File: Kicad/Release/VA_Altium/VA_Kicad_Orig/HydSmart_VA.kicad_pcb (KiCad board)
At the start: 4 copper layers, 36.6 x 24.8 mm, 23 parts, among them IC1 24FC04HT-I/OT, J1 TC2030-IDC-NL, J2 DNP, M1 AN54L15Q-U, U2 122, U3 CT8122AM-IS3, U4 CT8122AM-IS3, U5 112TR, U6 REG_BUCK_LowQ_6Vmax_150mA_1.8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, Y1 FC-135_32.7680KA-AG5

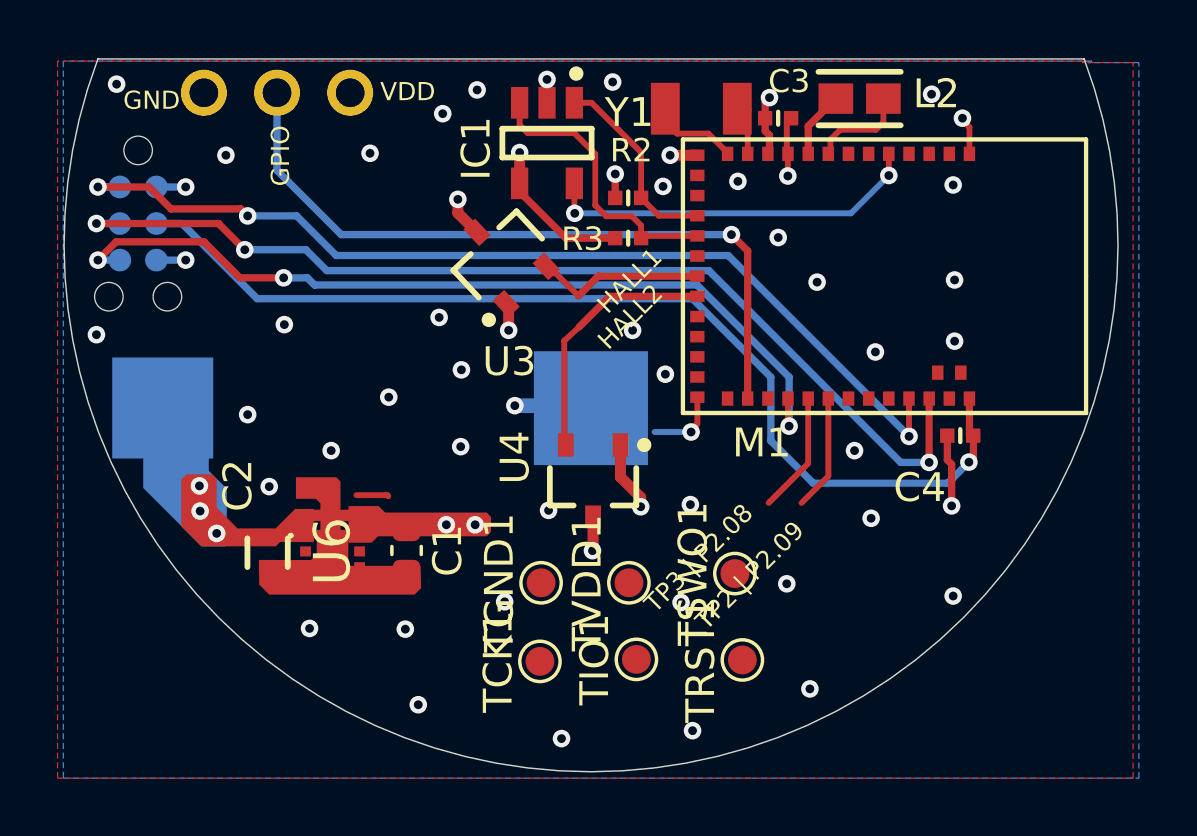
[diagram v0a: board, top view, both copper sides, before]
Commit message: VB changes start. Updated regulator and added test points
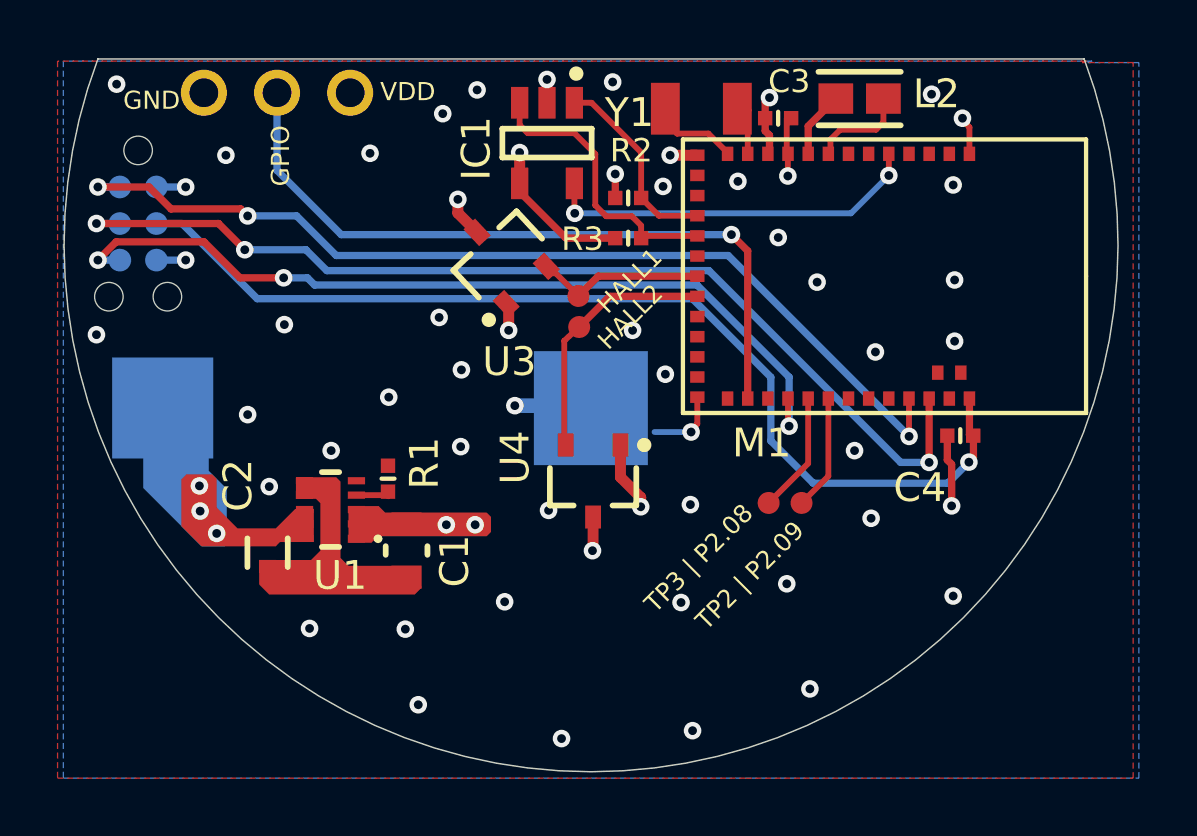
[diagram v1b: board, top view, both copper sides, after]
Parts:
- removed TCK1, TGND1, TIO1, TRST1, TSWO1, TVDD1: TestPoint, TestPoint:TestPoint_Pad_D1.0mm
- removed U6: REG_BUCK_LowQ_6Vmax_150mA_1.8V_XCL232D181KR-G, aa_footprints:XCL232B051KRG
- added ?: , HydSmart_VA:, F.Cu at (148.1, 101.9)
- added ?: , HydSmart_VA:, F.Cu at (148.1, 100.9)
- added ?: , HydSmart_VA:, F.Cu at (154.7, 108.0)
- added ?: , HydSmart_VA:, F.Cu at (155.8, 108.0)
- added R1: 20K, HydSmart_VA:R0402, F.Cu at (141.5, 107.2)
- added U1: MAXM38643AEMB+, HydSmart_VA:MAXM38643AEMB, F.Cu at (139.5, 108.3)
- C1: value 10uF_10V_0603 -> 47uF; footprint Capacitor_SMD:C_0603_1608Metric -> HydSmart_VA:FP-C2012-125-0_2-MFG
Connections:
- C1 pad 1: GND -> VDD
- C1 pad 2: VDD -> GND
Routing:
- net TP2: track 0.00 -> 4.19 mm
- net /Hydrosmart_NRF_MOD/TP2: track 4.19 -> 0.00 mm
- net TP1: track 0.00 -> 4.01 mm
- net /Hydrosmart_NRF_MOD/TP1: track 4.01 -> 0.00 mm
- net Net-(U1-RSEL): track 0.00 -> 1.12 mm
- net (no net): track 1.12 -> 0.00 mm
- net VDD: vias 6 -> 8
- net GND: vias 52 -> 50
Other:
- board text removed: "+"
- board text removed: "VB"
